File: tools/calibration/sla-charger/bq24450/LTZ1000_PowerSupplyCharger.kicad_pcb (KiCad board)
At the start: 2 copper layers, 75 x 50 mm, 52 parts, among them J1 Vin, J18 Battery, J19 Vout, J2 Charging, J3 PowerDispersion, Q1 BSS138, Q2 BC547, Q3 B C E, U1 BQ24450, U2 MIC2940, U3 TC54

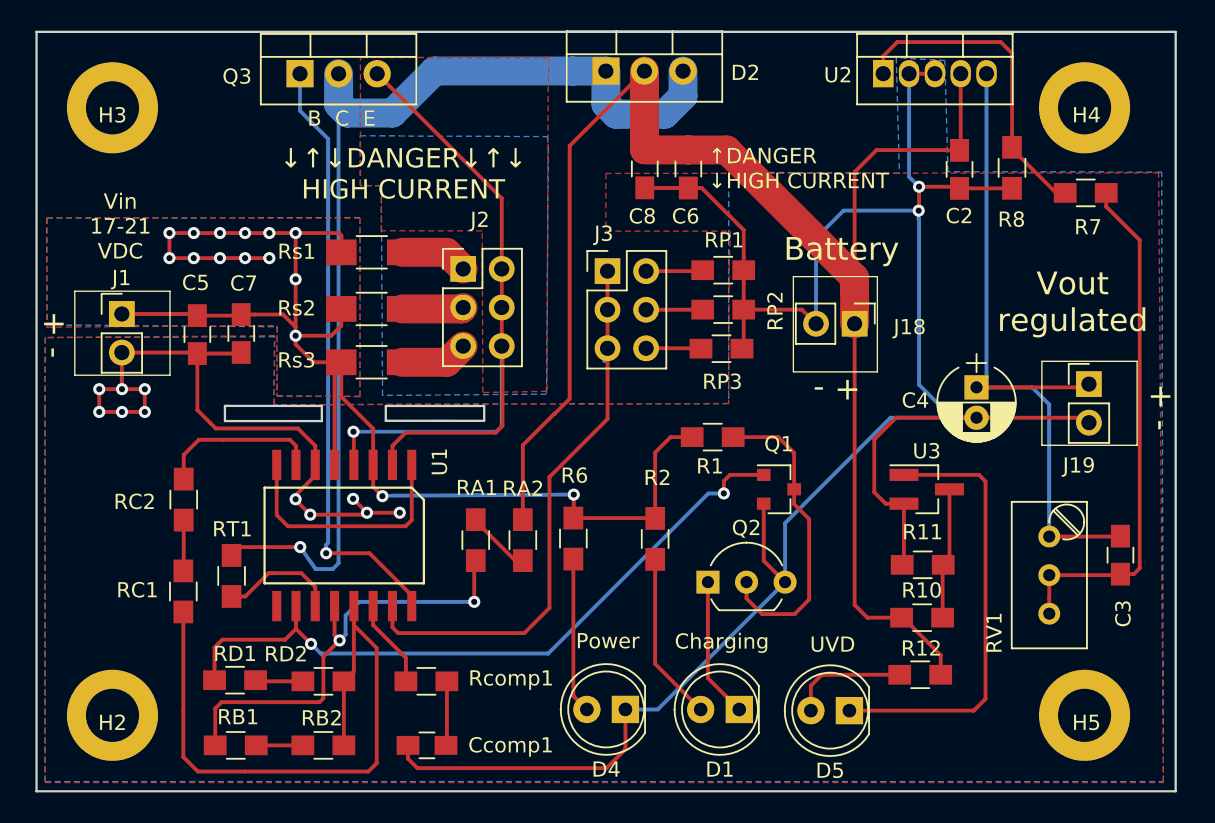
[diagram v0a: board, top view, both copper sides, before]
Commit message: Rev. C - Fixed issue when the power is switched on and the battery stayed in floating mode.   The issue was resolved with adding 1uF capacitor accross the Rdx resistors. - Changed Under Voltage Detector resistors divider values to fullfill >100uA requirement from the TC54 datasheet
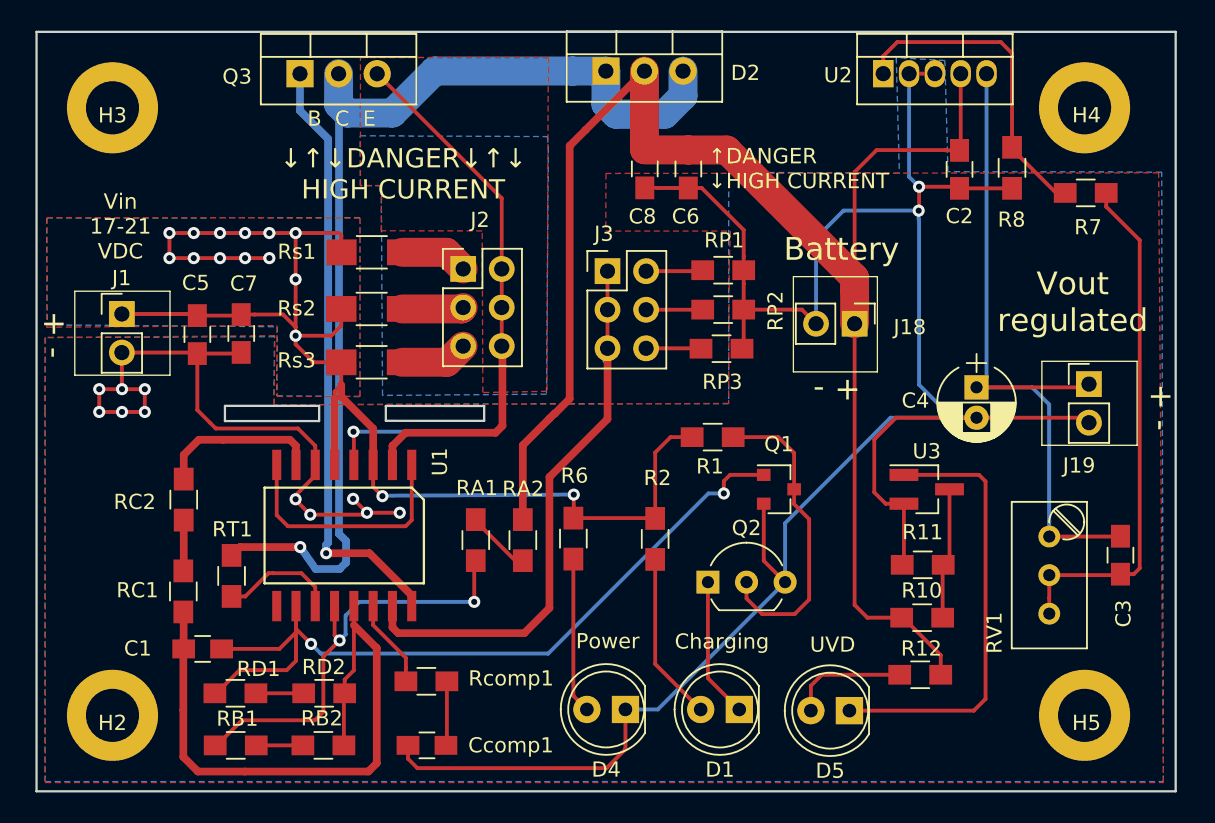
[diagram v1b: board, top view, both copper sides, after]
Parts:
- added C1: 1uF, Capacitors_SMD:C_0805_HandSoldering, F.Cu at (60.9, 90.6)
- R10: value 91K -> 45.3K
- R11: value 68K -> 28K
- moved RD1 0.86 mm to (63.1, 93.5)
- moved RD2 0.79 mm to (68.9, 93.5)
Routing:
- net STAT1: track 46.3 -> 52.0 mm
- net Vin: track 91.6 -> 90.1 mm
- net Net-(RA1-Pad1): track 29.9 -> 29.0 mm
- net Net-(D2-Pad1): track 71.1 -> 71.8 mm
- net Net-(C1-Pad1): track 43.3 -> 42.6 mm
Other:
- outline, holes or cut-outs redrawn
- board text added: "Designed by SEIDO CMT. Calibration Measurement Test. April 2019 Rev. C"
- board text removed: "Designed by SEIDO CMT. Calibration Measurement Test. March 2019 Rev. B"

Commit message: 1. Updated the calculation document. 2. Added schematics for custom I tapper value (not the defualt one 10% from charging current).    This will allow the PCB to be used in the cases when a load is connected to the battery. 3. Added polarity protection. 4. Increased track width.
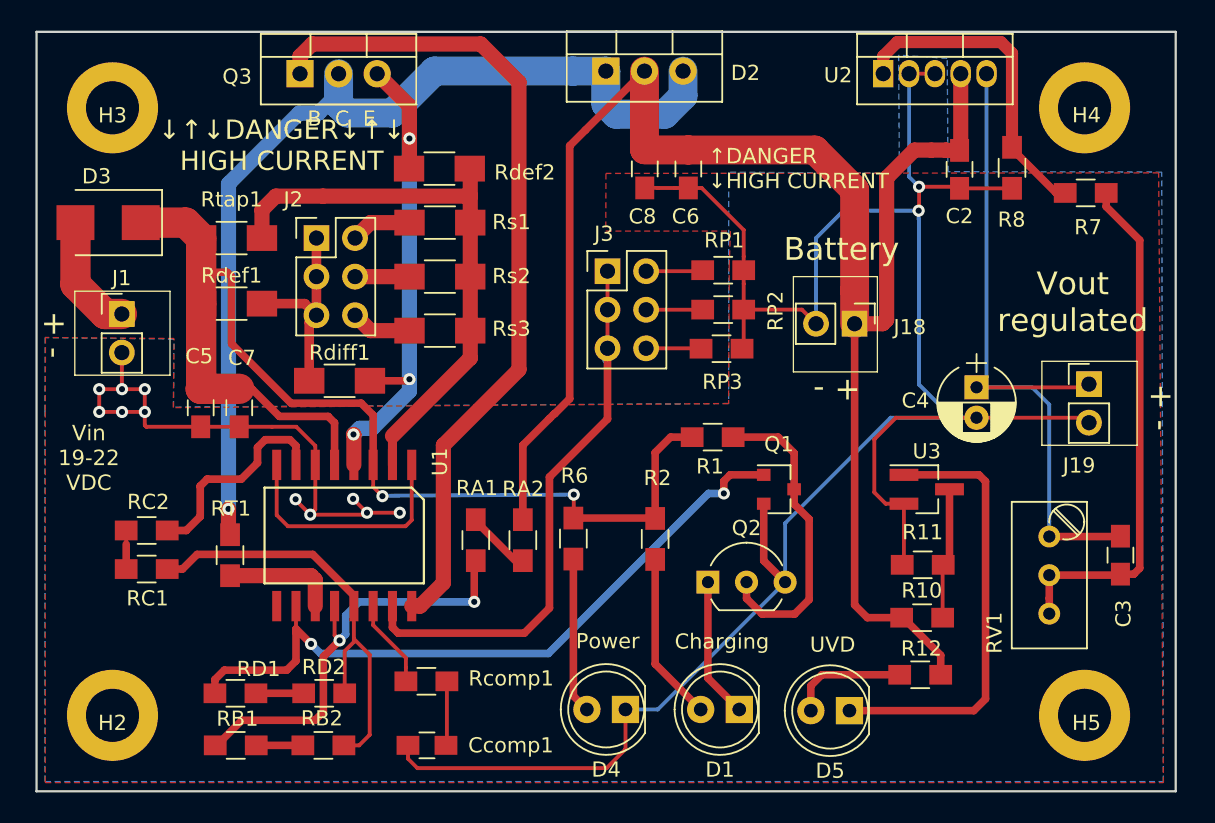
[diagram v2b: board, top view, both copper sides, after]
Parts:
- removed C1: 1uF, Capacitors_SMD:C_0805_HandSoldering
- added D3: D, LTZ1000_PowerSupplyCharger:D_SMB, F.Cu at (54.7, 62.6)
- added Rdef1: 0R, Resistors_SMD:R_1206_HandSoldering, F.Cu at (62.8, 67.9)
- added Rdef2: 0R, Resistors_SMD:R_1206_HandSoldering, F.Cu at (76.5, 59.0)
- added Rdiff1: 0R, Resistors_SMD:R_1206_HandSoldering, F.Cu at (70.0, 73.0)
- added Rtap1: 0R, Resistors_SMD:R_1206_HandSoldering, F.Cu at (62.8, 63.6)
- moved J2 9.87 mm to (68.4, 63.6)
- moved Rs2 4.97 mm to (76.6, 66.1)
- moved Rs3 4.95 mm to (76.6, 69.7)
- moved C7 4.89 mm to (63.3, 74.8)
- moved Rs1 4.89 mm to (76.6, 62.6)
- moved C5 4.83 mm to (60.8, 74.8)
- moved RC2 3.17 mm to (57.3, 82.8), turned to 180 degrees
- moved RC1 2.83 mm to (57.3, 85.4), turned to 0 degrees
- moved RT1 1.37 mm to (62.7, 84.5)
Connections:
- J1 pad 1: Vin -> Net-(D3-Pad2)
- J2 pad 2: Charge -> Net-(J2-Pad2)
- J2 pad 3: Net-(J2-Pad3) -> Net-(J2-Pad1)
- J2 pad 4: Charge -> Net-(J2-Pad4)
- J2 pad 5: Net-(J2-Pad5) -> Net-(J2-Pad1)
- J2 pad 6: Charge -> Net-(J2-Pad6)
- Q3 pad 3: Charge -> Net-(Q3-Pad3)
- Rs1 pad 1: Net-(J2-Pad1) -> Net-(Rdef2-Pad1)
- Rs1 pad 2: Vin -> Net-(J2-Pad2)
- Rs2 pad 1: Net-(J2-Pad3) -> Net-(Rdef2-Pad1)
- Rs2 pad 2: Vin -> Net-(J2-Pad4)
- Rs3 pad 1: Net-(J2-Pad5) -> Net-(Rdef2-Pad1)
- Rs3 pad 2: Vin -> Net-(J2-Pad6)
- U1 pad 2: Charge -> Net-(Rdef2-Pad1)
- U1 pad 4: Charge -> Net-(Q3-Pad3)
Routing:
- net Charge: track 52.4 -> 0.00 mm, vias 1 -> 0
- net Net-(Rdef2-Pad1): track 0.00 -> 37.6 mm
- net Net-(Q3-Pad3): track 0.00 -> 33.3 mm, vias 0 -> 3
- net Net-(Q3-Pad1): track 39.9 -> 54.7 mm, vias 1 -> 0
- net Net-(RB2-Pad1): track 42.6 -> 29.2 mm
- net Vin: track 90.1 -> 77.8 mm, vias 15 -> 2
- net Net-(J2-Pad1): track 4.47 -> 13.5 mm
- net Net-(D3-Pad2): track 0.00 -> 7.93 mm
- net Net-(D2-Pad1): track 71.8 -> 65.1 mm
- net GND: track 194.0 -> 187.6 mm
- net VBatt: track 105.9 -> 112.0 mm
- net STAT1: track 52.0 -> 47.2 mm
- net Net-(J2-Pad5): track 4.47 -> 0.00 mm
- net Net-(J2-Pad3): track 4.06 -> 0.00 mm
- net Net-(J2-Pad6): track 0.00 -> 4.01 mm
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- removed copper zone on B.Cu, net Charge
- removed copper zone on F.Cu, net Charge
- removed copper zone on B.Cu, net Vin
- removed copper zone on F.Cu, net Vin
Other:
- outline, holes or cut-outs redrawn
- board text added: "Designed by SEIDO CMT. Calibration Measurement Test. May 2019 Rev. D"
- board text added: "Vin 19-22 VDC"
- board text removed: "Designed by SEIDO CMT. Calibration Measurement Test. April 2019 Rev. C"
- board text removed: "Vin 17-21 VDC"
